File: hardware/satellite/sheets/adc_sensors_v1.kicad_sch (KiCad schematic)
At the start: 7 parts, among them J2 Conn_01x03, J3 Conn_01x03, J4 Conn_01x03, J5 Conn_01x03, U2 ADS1115IDGS

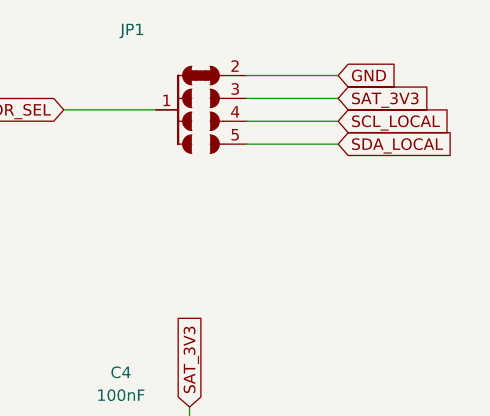
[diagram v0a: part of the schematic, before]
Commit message: hardware(satellite): rev 1.1, larger address jumpers, qwiic moved clear of PCA9615
- JP1: enlarge footprint to 9.5 x 8.5 mm (2.0 mm row pitch, 2.0 x 1.2 mm
  pads) for easier solder and cut. Reorder pins 4/5 so the silkscreen and
  symbol read in address order: pin 4 = SDA = 0x4A, pin 5 = SCL = 0x4B.
  The silkscreen previously had 0x4A/0x4B swapped against the nets.
- JP16: enlarge footprint to 5.5 x 6.5 mm courtyard with larger pads.
- Move the qwiic port away from the PCA9615DPZ so hot-air rework of the
  buffer no longer melts the connector.
- Add the PCA9615 recommended TSSOP10 footprint and use it on U4.
- Add ohm signs to resistor values; update one termination value.
- Bump REV_NUM to 1.1.
- Update the ADS1115 and net-connection docs for the swapped JP1 pins.

Co-Authored-By: Claude Sonnet 5.5 <noreply@anthropic.com>
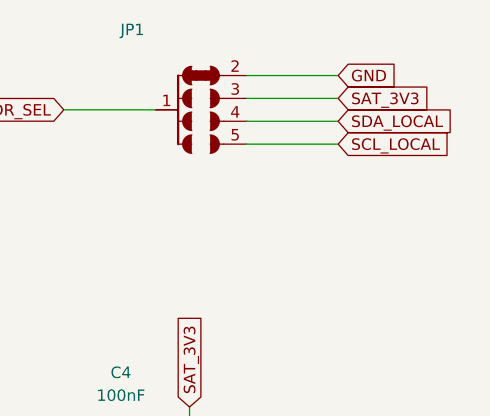
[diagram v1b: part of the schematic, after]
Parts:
- JP1: Usage 4-way address selector solder jumper block (Pin 1: ADDR; Pin 2: GND for 0x48 default bridged; Pin 3: SAT_3V3 for 0x49; Pin 4: SCL for 0x4B; Pin 5: SDA for 0x4A) -> 4-way address selector solder jumper block (Pin 1: ADDR; Pin 2: GND for 0x48 default bridged; Pin 3: SAT_3V3 for 0x49; Pin 4: SDA for 0x4A; Pin 5: SCL for 0x4B)
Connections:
- net SCL_LOCAL: now also JP1.5 (0x4B); no longer JP1.4 (0x4B)
- net SDA_LOCAL: now also JP1.4 (0x4A); no longer JP1.5 (0x4A)
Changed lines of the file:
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@@
+		)
+	)
+	(global_label "SDA_LOCAL"
+		(shape input)
+		(at 177.8 52.07 0)
+		(effects
+			(font
+				(size 1.27 1.27)
+			)
+			(justify left)
+		)
+		(property "Intersheetrefs" "${INTERSHEET_REFS}"
+			(at 177.8 52.07 0)
+			(hide yes)
+			(show_name no)
+			(do_not_autoplace no)
+			(effects
+				(font
+					(size 1.27 1.27)
+				)
+			)
 		)
 	)
@@
 		)
 	)
+	(global_label "GND"
+		(shape input)
+		(at 40.64 88.9 180)
+		(effects
+			(font
+				(size 1.27 1.27)
+			)
+			(justify right)
+		)
+		(property "Intersheetrefs" "${INTERSHEET_REFS}"
+			(at 40.64 88.9 0)
+			(hide yes)
+			(show_name no)
+			(do_not_autoplace no)
+			(effects
+				(font
+					(size 1.27 1.27)
+				)
+			)
+		)
+	)
 	(global_label "SCL_LOCAL"
 		(shape input)
-		(at 177.8 52.07 0)
-		(effects
-			(font
-				(size 1.27 1.27)
-			)
-			(justify left)
-		)
-		(property "Intersheetrefs" "${INTERSHEET_REFS}"
-			(at 177.8 52.07 0)
+		(at 121.92 76.2 0)
+		(effects
+			(font
+				(size 1.27 1.27)
+			)
+			(justify left)
+		)
+		(property "Intersheetrefs" "${INTERSHEET_REFS}"
+			(at 121.92 76.2 0)
+			(hide yes)
+			(show_name no)
+			(do_not_autoplace no)
+			(effects
+				(font
+					(size 1.27 1.27)
+				)
+			)
+		)
+	)
+	(global_label "ADDR_SEL"
+		(shape input)
+		(at 147.32 50.8 180)
+		(effects
+			(font
+				(size 1.27 1.27)
+			)
+			(justify right)
+		)
+		(property "Intersheetrefs" "${INTERSHEET_REFS}"
+			(at 147.32 50.8 0)
+			(hide yes)
+			(show_name no)
+			(do_not_autoplace no)
+			(effects
+				(font
+					(size 1.27 1.27)
+				)
+			)
+		)
+	)
+	(global_label "MOIST3"
+		(shape input)
+		(at 81.28 78.74 180)
+		(effects
+			(font
+				(size 1.27 1.27)
+			)
+			(justify right)
+		)
+		(property "Intersheetrefs" "${INTERSHEET_REFS}"
+			(at 81.28 78.74 0)
+			(hide yes)
+			(show_name no)
+			(do_not_autoplace no)
+			(effects
+				(font
+					(size 1.27 1.27)
+				)
+			)
+		)
+	)
+	(global_label "MOIST1"
+		(shape input)
+		(at 40.64 68.58 180)
+		(effects
+			(font
+				(size 1.27 1.27)
+			)
+			(justify right)
+		)
+		(property "Intersheetrefs" "${INTERSHEET_REFS}"
+			(at 40.64 68.58 0)
+			(hide yes)
+			(show_name no)
+			(do_not_autoplace no)
+			(effects
+				(font
+					(size 1.27 1.27)
+				)
+			)
+		)
+	)
+	(global_label "MOIST4"
+		(shape input)
+		(at 40.64 144.78 180)
+		(effects
+			(font
+				(size 1.27 1.27)
+			)
+			(justify right)
+		)
+		(property "Intersheetrefs" "${INTERSHEET_REFS}"
+			(at 40.64 144.78 0)
 			(hide yes)
 			(show_name no)
@@
 	(global_label "GND"
 		(shape input)
-		(at 40.64 88.9 180)
-		(effects
-			(font
-				(size 1.27 1.27)
-			)
-			(justify right)
-		)
-		(property "Intersheetrefs" "${INTERSHEET_REFS}"
-			(at 40.64 88.9 0)
+		(at 101.6 96.52 270)
+		(effects
+			(font
+				(size 1.27 1.27)
+			)
+			(justify right)
+		)
+		(property "Intersheetrefs" "${INTERSHEET_REFS}"
+			(at 101.6 96.52 0)
 			(hide yes)
 			(show_name no)
@@
 	(global_label "SCL_LOCAL"
 		(shape input)
-		(at 121.92 76.2 0)
-		(effects
-			(font
-				(size 1.27 1.27)
-			)
-			(justify left)
-		)
-		(property "Intersheetrefs" "${INTERSHEET_REFS}"
-			(at 121.92 76.2 0)
-			(hide yes)
-			(show_name no)
-			(do_not_autoplace no)
-			(effects
-				(font
-					(size 1.27 1.27)
-				)
-			)
-		)
-	)
-	(global_label "ADDR_SEL"
-		(shape input)
-		(at 147.32 50.8 180)
-		(effects
-			(font
-				(size 1.27 1.27)
-			)
-			(justify right)
-		)
-		(property "Intersheetrefs" "${INTERSHEET_REFS}"
-			(at 147.32 50.8 0)
-			(hide yes)
-			(show_name no)
-			(do_not_autoplace no)
-			(effects
-				(font
-					(size 1.27 1.27)
-				)
-			)
-		)
-	)
-	(global_label "MOIST3"
-		(shape input)
-		(at 81.28 78.74 180)
-		(effects
-			(font
-				(size 1.27 1.27)
-			)
-			(justify right)
-		)
-		(property "Intersheetrefs" "${INTERSHEET_REFS}"
-			(at 81.28 78.74 0)
-			(hide yes)
-			(show_name no)
-			(do_not_autoplace no)
-			(effects
-				(font
-					(size 1.27 1.27)
-				)
-			)
-		)
-	)
-	(global_label "MOIST1"
-		(shape input)
-		(at 40.64 68.58 180)
-		(effects
-			(font
-				(size 1.27 1.27)
-			)
-			(justify right)
-		)
-		(property "Intersheetrefs" "${INTERSHEET_REFS}"
-			(at 40.64 68.58 0)
-			(hide yes)
-			(show_name no)
-			(do_not_autoplace no)
-			(effects
-				(font
-					(size 1.27 1.27)
-				)
-			)
-		)
-	)
-	(global_label "MOIST4"
-		(shape input)
-		(at 40.64 144.78 180)
-		(effects
-			(font
-				(size 1.27 1.27)
-			)
-			(justify right)
-		)
-		(property "Intersheetrefs" "${INTERSHEET_REFS}"
-			(at 40.64 144.78 0)
-			(hide yes)
-			(show_name no)
-			(do_not_autoplace no)
-			(effects
-				(font
-					(size 1.27 1.27)
-				)
-			)
-		)
-	)
-	(global_label "SDA_LOCAL"
-		(shape input)
 		(at 177.8 54.61 0)
 		(effects
@@
 		(property "Intersheetrefs" "${INTERSHEET_REFS}"
 			(at 177.8 54.61 0)
-			(hide yes)
-			(show_name no)
-			(do_not_autoplace no)
-			(effects
-				(font
-					(size 1.27 1.27)
-				)
-			)
-		)
-	)
-	(global_label "GND"
-		(shape input)
-		(at 101.6 96.52 270)
-		(effects
-			(font
-				(size 1.27 1.27)
-			)
-			(justify right)
-		)
-		(property "Intersheetrefs" "${INTERSHEET_REFS}"
-			(at 101.6 96.52 0)
 			(hide yes)
 			(show_name no)
@@
 			)
 		)
-		(property "Usage" "4-way address selector solder jumper block (Pin 1: ADDR; Pin 2: GND for 0x48 default bridged; Pin 3: SAT_3V3 for 0x49; Pin 4: SCL for 0x4B; Pin 5: SDA for 0x4A)"
+		(property "Usage" "4-way address selector solder jumper block (Pin 1: ADDR; Pin 2: GND for 0x48 default bridged; Pin 3: SAT_3V3 for 0x49; Pin 4: SDA for 0x4A; Pin 5: SCL for 0x4B)"
 			(at 162.56 50.8 0)
 			(hide yes)
